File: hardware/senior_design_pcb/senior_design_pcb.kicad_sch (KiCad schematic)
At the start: 62 parts, among them J1 SBH11-PBPC-D05-ST-BK, J10 1x06Screw-Stepper Driver2, J11 2x08Rectangle-LED Matrix Conn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, J12 1x05JST - Joystick2 connector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, J13 UJ20-C-H-C-4-SMT-TR, J3 1x02JST-IR Transmitter1, J4 1x03JST- IR Receiver1, J5 1x05JST-Admin LCD Console Con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, J6 1x05JST - Joystick1 connector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, J7 1x02JST-IR Transmitter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

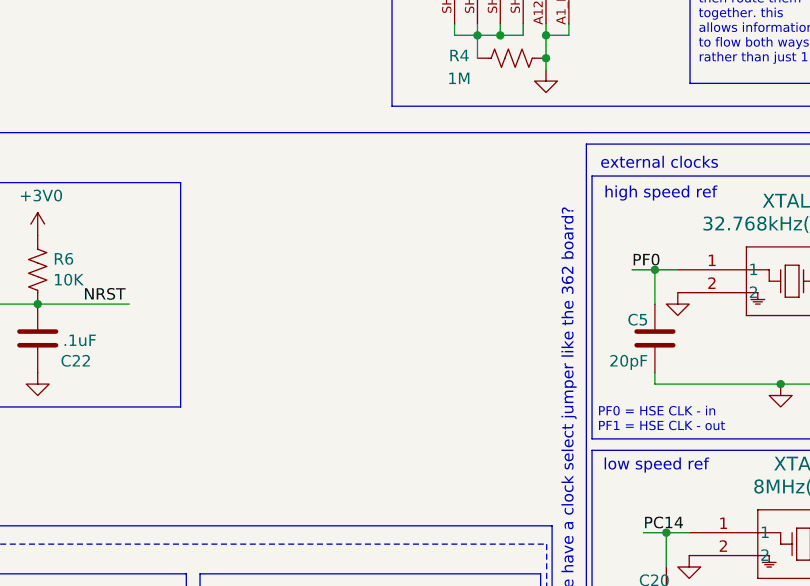
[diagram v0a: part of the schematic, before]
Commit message: added unused pin header
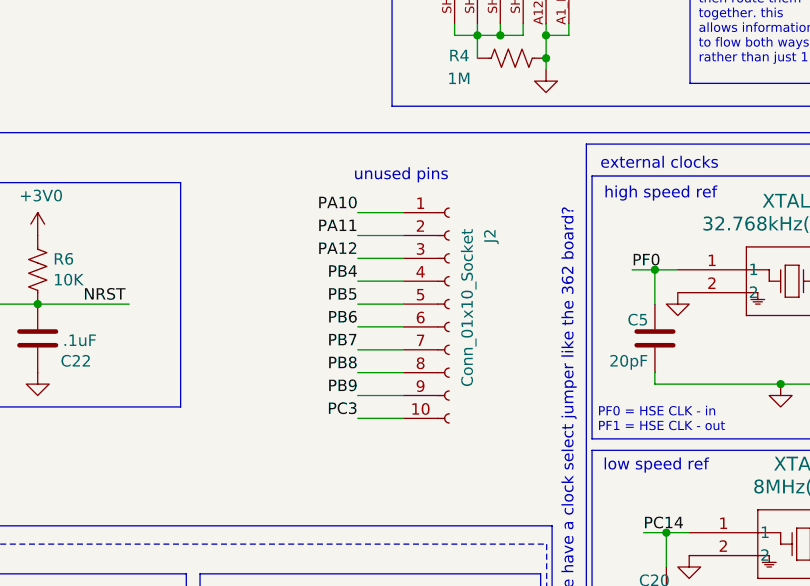
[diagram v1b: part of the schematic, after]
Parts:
- added J2: Conn_01x10_Socket, symbol Connector:Conn_01x10_Socket
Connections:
- net PA10: now also J2.1 (Pin_1)
- net PA11: now also J2.2 (Pin_2)
- net PA12: now also J2.3 (Pin_3)
- net PB4: now also J2.4 (Pin_4)
- net PB5: now also J2.5 (Pin_5)
- net PB6: now also J2.6 (Pin_6)
- net PB7: now also J2.7 (Pin_7)
- net PB8: now also J2.8 (Pin_8)
- net PB9: now also J2.9 (Pin_9)
- net PC3: now also J2.10 (Pin_10)
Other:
- note added: "unused pins"

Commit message: added a lot of comments for clarity
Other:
- note added: "notes:"
- company: (none) -> Purdue University ECE49595
- title: AutonAir STM -> AutonAir
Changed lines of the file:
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@@
 	(paper "USLegal")
 	(title_block
-		(title "AutonAir STM")
+		(title "AutonAir")
+		(company "Purdue University ECE49595")
 	)
 	(rectangle
@@
 		)
 	)
+	(text "notes:"
+		(exclude_from_sim no)
+		(at -37.592 27.178 0)
+		(effects
+			(font
+				(size 1.27 1.27)
+			)
+		)
+	)
 	(text "high speed ref"
 		(exclude_from_sim no)
@@
 		)
 	)
+	(text_box "we might change some of these pinouts. nandan says its hard to program but i fear that it will be impossible to route if we make them all sequential according to name. we will talk in our meeting tomorrow tho"
+		(exclude_from_sim no)
+		(at 34.29 -3.81 0)
+		(size 36.83 17.78)
+		(margins 0.9525 0.9525 0.9525 0.9525)
+		(stroke
+			(width 0)
+			(type solid)
+		)
+		(fill
+			(type none)
+		)
+		(effects
+			(font
+				(size 1.27 1.27)
+			)
+			(justify left top)
+		)
+	)
 	(text_box "this button right here is the one built into the joystick. it wont be added to the PCB or anything"
 		(exclude_from_sim no)
@@
 		)
 	)
+	(text_box "vias 15 mils hole diameter\nuntinted vias for tp\n\n"
+		(exclude_from_sim no)
+		(at -40.64 66.04 0)
+		(size 27.94 19.05)
+		(margins 0.9525 0.9525 0.9525 0.9525)
+		(stroke
+			(width 0)
+			(type solid)
+		)
+		(fill
+			(type none)
+		)
+		(effects
+			(font
+				(size 1.27 1.27)
+			)
+			(justify left top)
+		)
+	)
 	(text_box "these do share a ground with the STM already :)"
 		(exclude_from_sim no)
@@
 		)
 	)
+	(text_box "This is the big square JTAG on the 362 pcb. we will carry it over since we aready have the STLinkV2 connector for it."
+		(exclude_from_sim no)
+		(at 124.46 67.31 0)
+		(size 27.94 15.24)
+		(margins 0.9525 0.9525 0.9525 0.9525)
+		(stroke
+			(width 0)
+			(type solid)
+		)
+		(fill
+			(type none)
+		)
+		(effects
+			(font
+				(size 1.27 1.27)
+			)
+			(justify left top)
+		)
+	)
 	(text_box "this is the 5v status LED"
 		(exclude_from_sim no)
@@
 		)
 	)
+	(text_box "Status Light here :)"
+		(exclude_from_sim no)
+		(at 330.2 118.11 0)
+		(size 25.4 5.08)
+		(margins 0.9525 0.9525 0.9525 0.9525)
+		(stroke
+			(width 0)
+			(type solid)
+		)
+		(fill
+			(type none)
+		)
+		(effects
+			(font
+				(size 1.27 1.27)
+			)
+			(justify left top)
+		)
+	)
 	(text_box "These should have external power according to Nandan. They should share a common ground though."
 		(exclude_from_sim no)
@@
 			)
 			(justify left top)
+		)
+	)
+	(text_box "These are the decoupling caps. I keep them over here because it is so messy otherwise.\ntheyre seperated by which pin group they go to. each section has a bulk cap to put near the usbc\n"
+		(exclude_from_sim no)
+		(at 340.36 140.97 0)
+		(size 38.1 13.97)
+		(margins 0.9525 0.9525 0.9525 0.9525)
+		(stroke
+			(width 0)
+			(type solid)
+		)
+		(fill
+			(type none)
+		)
+		(effects
+			(font
+				(size 1.27 1.27)
+			)
+			(justify left top)
+		)
+	)
+	(text_box "USB->UART Bridge. The chip we use has no programming pins used. I looked into it and it also does not get programmed before iirc. we should be good to run it as it is default.\n"
+		(exclude_from_sim no)
+		(at 250.19 68.58 0)
+		(size 25.4 19.05)
+		(margins 0.9525 0.9525 0.9525 0.9525)
+		(stroke
+			(width 0)
+			(type solid)
+		)
+		(fill
+			(type none)
+		)
+		(effects
+			(font
+				(size 1.27 1.27)
+			)
+			(justify left top)

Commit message: more comments <3
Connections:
- net +24V: no longer names the net of J10.1 (Pin_1)
- net +24V: no longer J9.1 (Pin_1)
- no-connect marks 27 -> 31
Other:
- note added: "in that case should these just be 1:5 instead of 1:6"

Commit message: edited schematic pinouts
added test points
edited pinouts for easier traces
added header
added comments
+notes from class today & what to change
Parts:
- removed J2: Conn_01x10_Socket, symbol Connector:Conn_01x10_Socket
- added J2: Conn_01x08_Pin, Connector_PinHeader_2.54mm:PinHeader_1x08_P2.54mm_Vertical, symbol Connector:Conn_01x08_Pin
- added TP1: TestPoint_Small, TestPoint:TestPoint_Pad_D1.5mm, symbol Connector:TestPoint_Small
- added TP2: TestPoint, TestPoint:TestPoint_THTPad_D1.5mm_Drill0.7mm, symbol testpoint:TestPoint
- added TP3: NRST, TestPoint:TestPoint_THTPad_D1.5mm_Drill0.7mm, symbol testpoint:TestPoint
- added TP4: IR-IN1, TestPoint:TestPoint_THTPad_D1.5mm_Drill0.7mm, symbol testpoint:TestPoint
- added TP5: IR-IN2, TestPoint:TestPoint_THTPad_D1.5mm_Drill0.7mm, symbol testpoint:TestPoint
- added TP6: VBUS, TestPoint:TestPoint_THTPad_D1.5mm_Drill0.7mm, symbol testpoint:TestPoint
- added TP7: +5V, TestPoint:TestPoint_THTPad_D1.5mm_Drill0.7mm, symbol testpoint:TestPoint
- added TP8: 3V3, TestPoint:TestPoint_THTPad_D1.5mm_Drill0.7mm, symbol testpoint:TestPoint
- added TP9: GND, TestPoint:TestPoint_THTPad_D1.5mm_Drill0.7mm, symbol testpoint:TestPoint
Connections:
- net PA11 is gone; now on net IR_IN_2: U2.44 (PA11)
- net PA12 is gone; now on net IR_IN_1: U2.45 (PA12)
- net PB4 is gone; now on net ADMIN_CONSOLE-BUTTON: U2.56 (PB4)
- net +3V0: now also TP8.1
- net +5V: now also TP7.1
- net A: now also U2.26 (PB0); no longer U2.24 (PC4)
- net ADMIN_CONSOLE-BUTTON: no longer U2.55 (PB3)
- net B: now also U2.27 (PB1); no longer U2.23 (PA7)
- net B1: now also U2.22 (PA6); no longer U2.28 (PB2)
- net C: now also U2.29 (PB10); no longer U2.22 (PA6)
- net CLK: now also U2.33 (PB12); no longer U2.20 (PA4)
- net D: now also U2.30 (PB11); no longer U2.21 (PA5)
- net G1: now also U2.21 (PA5); no longer U2.29 (PB10)
- net G2: now also U2.24 (PC4); no longer U2.26 (PB0)
- net GND: now also TP9.1
- net IR_IN_1: now also TP4.1; no longer U2.42 (PA9)
- net IR_IN_2: now also TP5.1; no longer U2.41 (PA8)
- net LAT: now also U2.34 (PB13); no longer U2.17 (PA3)
- net NRST: now also TP3.1
- net OE: now also U2.35 (PB14); no longer U2.16 (PA2)
- net PA0: now also J2.7 (Pin_7); no longer J12.3 (Pin_3)
- net PA1: now also J2.8 (Pin_8); no longer J12.4 (Pin_4)
- net PA10: now also J9.2 (Pin_2)
- net PB15: now also J10.5 (Pin_5); no longer J9.5 (Pin_5)
- net PB5: now also J2.1 (Pin_1)
- net PB6: now also J2.2 (Pin_2)
- net PB7: now also J2.3 (Pin_3)
- net PB8: now also J2.4 (Pin_4)
- net PB9: now also J2.5 (Pin_5)
- net PC3: now also J2.6 (Pin_6)
- net PC6: now also J10.4 (Pin_4); no longer J10.2 (Pin_2)
- net PC8: now also J10.2 (Pin_2); no longer J10.4 (Pin_4)
- net PC9: now also J9.5 (Pin_5); no longer J10.5 (Pin_5)
- net VBUS: now also TP6.1
- net usbc-shield: now reaches J13.SH1 (SHIELD), J13.SH2 (SHIELD__1), J13.SH3 (SHIELD__2), J13.SH4 (SHIELD__3), R4.1
- net cc2: now reaches J13.B5 (CC2), R2.1
- net cc1: now reaches J13.A5 (CC1), R1.1
- net PB1 renamed PA7
- net PA7: now also U2.23 (PA7); no longer U2.27 (PB1)
- net PB11 renamed PA4
- net PA4: now also U2.20 (PA4); no longer U2.30 (PB11)
- removed net PB12: J9.2 (Pin_2), U2.33 (PB12)
- net PB13 renamed PA9
- net PA9: now also U2.42 (PA9); no longer U2.34 (PB13)
- net PB14 renamed PA8
- net PA8: now also U2.41 (PA8); no longer U2.35 (PB14)
- new net PA2: J12.3 (Pin_3), U2.16 (PA2)
- new net PA3: J12.4 (Pin_4), U2.17 (PA3)
- new net PB2: U2.28 (PB2)
- new net PB3: U2.55 (PB3)
- no-connect marks 31 -> 21
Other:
- note added: "two diff kinds of tp - pad (left) and drill hole (right):"
- note removed: "notes:"
- moved on the sheet: C1, C2, C3, C4, FB1, FT1, J13, R1, R2, R4

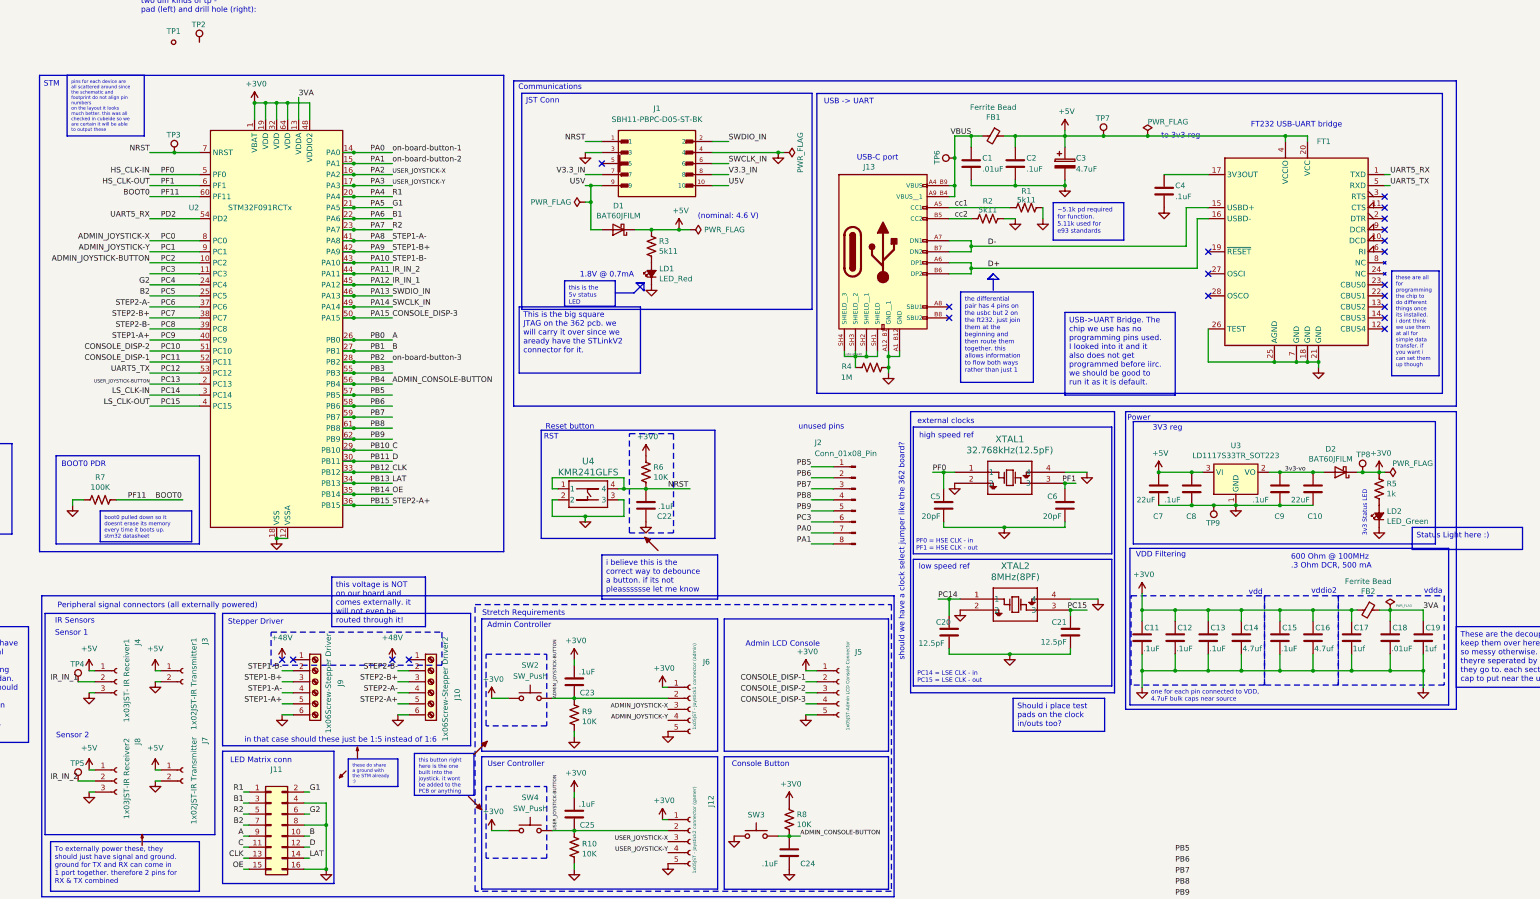
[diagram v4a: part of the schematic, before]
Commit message: decoupling caps and diffe pair
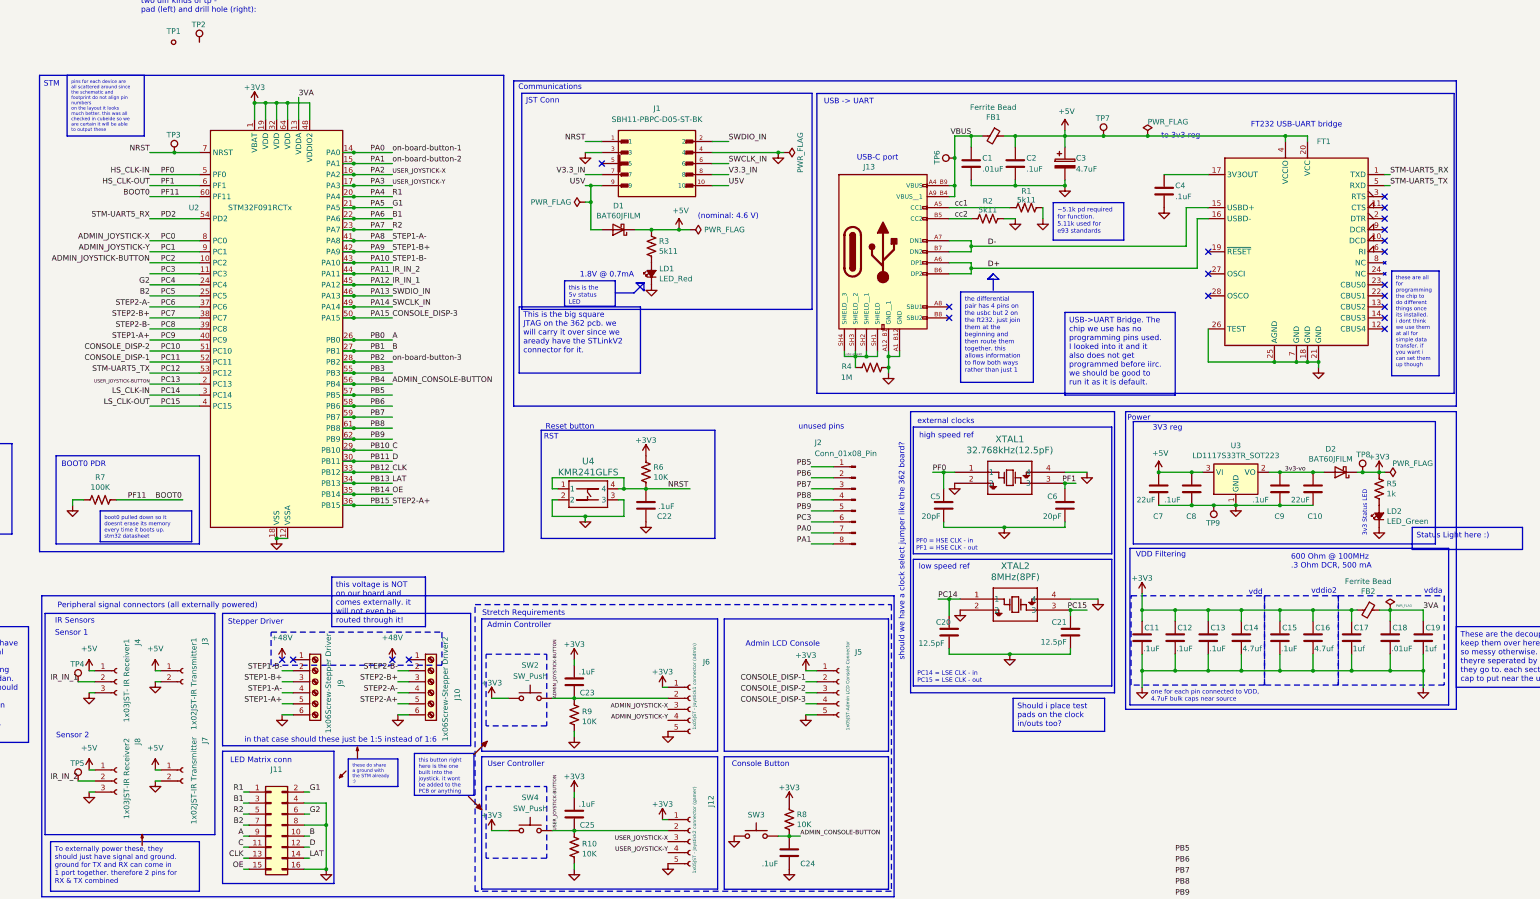
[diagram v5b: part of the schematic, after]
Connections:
- net +3V0 renamed +3V3
